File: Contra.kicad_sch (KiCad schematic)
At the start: 100 parts, among them J1 Conn_01x04, SW1 SW_PUSH, U1 ProMicro

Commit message: update keyswitch symbol
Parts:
- MX1, MX10, MX11, MX12, MX13, MX14, MX15, MX16, MX17, MX18, MX19, MX2, MX20, MX21, MX22, MX23, MX24, MX25, MX26, MX27, MX28, MX29, MX3, MX30, MX31, MX32, MX33, MX34, MX35, MX36, MX37, MX38, MX39, MX4, MX40, MX41, MX42, MX43, MX44, MX45, MX46, MX47, MX48, MX5, MX6, MX7, MX8, MX9: symbol MX_Alps_Hybrids:MX-1U -> keyboard_parts:KEYSW

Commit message: update keyswitch matrix
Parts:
- MX49: symbol MX_Alps_Hybrids:MX-2U -> keyboard_parts:KEYSW
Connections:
- net COL0: now also MX1.1, MX13.1, MX25.1, MX37.1
- net COL1: now also MX14.1, MX2.1, MX26.1, MX38.1
- net COL10: now also MX11.1, MX23.1, MX35.1, MX47.1
- net COL11: now also MX12.1, MX24.1, MX36.1, MX48.1
- net COL2: now also MX15.1, MX27.1, MX3.1, MX39.1
- net COL3: now also MX16.1, MX28.1, MX4.1, MX40.1
- net COL4: now also MX17.1, MX29.1, MX41.1, MX5.1
- net COL5: now also MX18.1, MX30.1, MX42.1, MX6.1
- net COL6: now also MX19.1, MX31.1, MX43.1, MX7.1
- net COL7: now also MX20.1, MX32.1, MX44.1, MX8.1
- net COL8: now also MX21.1, MX33.1, MX45.1, MX9.1
- net COL9: now also MX10.1, MX22.1, MX34.1, MX46.1
- net at MX1.2: now also D1.2 (A)
- net at MX2.2: now also D2.2 (A)
- net at MX3.2: now also D3.2 (A)
- net at MX4.2: now also D4.2 (A)
- net at MX5.2: now also D5.2 (A)
- net at MX6.2: now also D6.2 (A)
- net at MX7.2: now also D7.2 (A)
- net at MX8.2: now also D8.2 (A)
- net at MX9.2: now also D9.2 (A)
- net at MX10.2: now also D10.2 (A)
- net at MX11.2: now also D11.2 (A)
- net at MX12.2: now also D12.2 (A)
- net at MX13.2: now also D13.2 (A)
- net at MX14.2: now also D14.2 (A)
- net at MX15.2: now also D15.2 (A)
- net at MX16.2: now also D16.2 (A)
- net at MX17.2: now also D17.2 (A)
- net at MX18.2: now also D18.2 (A)
- net at MX19.2: now also D19.2 (A)
- net at MX20.2: now also D20.2 (A)
- net at MX21.2: now also D21.2 (A)
- net at MX22.2: now also D22.2 (A)
- net at MX23.2: now also D23.2 (A)
- net at MX24.2: now also D24.2 (A)
- net at MX25.2: now also D25.2 (A)
- net at MX26.2: now also D26.2 (A)
- net at MX27.2: now also D27.2 (A)
- net at MX28.2: now also D28.2 (A)
- net at MX29.2: now also D29.2 (A)
- net at MX30.2: now also D30.2 (A)
- net at MX31.2: now also D31.2 (A)
- net at MX32.2: now also D32.2 (A)
- net at MX33.2: now also D33.2 (A)
- net at MX34.2: now also D34.2 (A)
- net at MX35.2: now also D35.2 (A)
- net at MX36.2: now also D36.2 (A)
- net at MX37.2: now also D37.2 (A)
- net at MX38.2: now also D38.2 (A)
- net at MX39.2: now also D39.2 (A)
- net at MX40.2: now also D40.2 (A)
- net at MX41.2: now also D41.2 (A)
- net at MX42.2: now also D42.2 (A)
- net at MX43.2: now also D43.2 (A)
- net at MX44.2: now also D44.2 (A)
- net at MX45.2: now also D45.2 (A)
- net at MX46.2: now also D46.2 (A)
- net at MX47.2: now also D47.2 (A)
- net at MX48.2: now also D48.2 (A)
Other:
- note added: "Accessory Jumper"
- note added: "Keyswitch Matrix"
- note added: "MCU Connections"
- moved on the sheet: D1, D10, D11, D12, D13, D14, D15, D16, D17, D18, D19, D2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

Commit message: update foot prints to be hotswap sockets
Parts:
- D1, D10, D11, D12, D13, D14, D15, D16, D17, D18, D19, D2, D20, D21, D22, D23, D24, D25, D26, D27, D28, D29, D3, D30, D31, D32, D33, D34, D35, D36, D37, D38, D39, D4, D40, D41, D42, D43, D44, D45, D46, D47, D48, D5, D6, D7, D8, D9: footprint locallib:D_DO-35_SOD27_P7.62mm_Horizontal-DoubleSided -> Diode_THT:D_DO-35_SOD27_P7.62mm_Horizontal
- J1: footprint Pin_Headers:Pin_Header_Straight_1x04_Pitch2.54mm -> Connector_PinHeader_2.54mm:PinHeader_1x04_P2.54mm_Horizontal
- MX1, MX10, MX11, MX12, MX13, MX14, MX15, MX16, MX17, MX18, MX19, MX2, MX20, MX21, MX22, MX23, MX24, MX25, MX26, MX27, MX28, MX29, MX3, MX30, MX31, MX32, MX33, MX34, MX35, MX36, MX37, MX38, MX39, MX4, MX40, MX41, MX42, MX43, MX44, MX45, MX46, MX47, MX48, MX5, MX6, MX7, MX8, MX9: footprint MX_Alps_Hybrid:MX-1U-NoLED -> MX_Hotswap:MX-Hotswap-1U
- MX49: footprint MX_Alps_Hybrid:MX-2U-ReversedStabilizers-NoLED -> MX_Hotswap:MX-Hotswap-2U-ReversedStabilizers
- SW1: footprint Molex-0548190589:PushButton_6x6mm_TH_Pretty -> Button_Switch_THT:SW_PUSH_1P1T_6x3.5mm_H5.0_APEM_MJTP1250

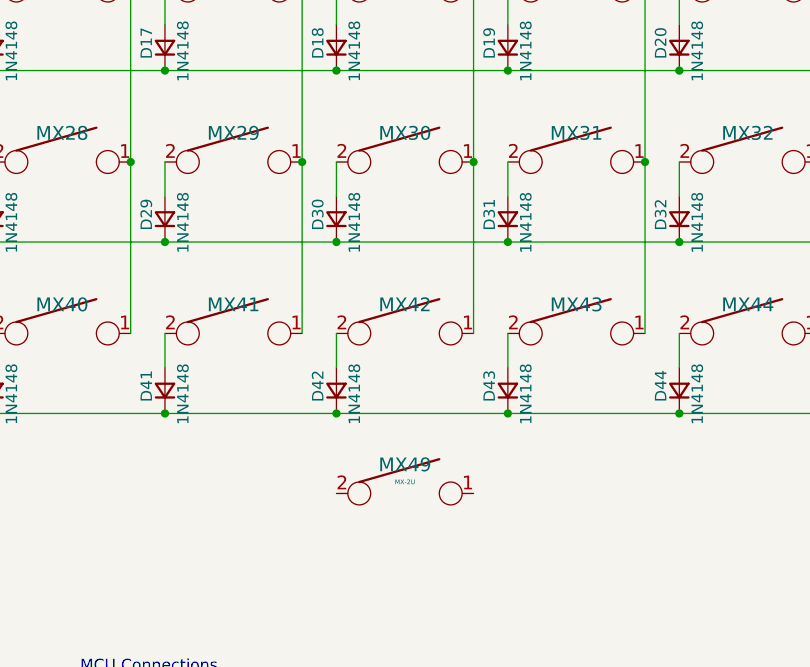
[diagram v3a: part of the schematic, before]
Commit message: place switch 49 in the correct place
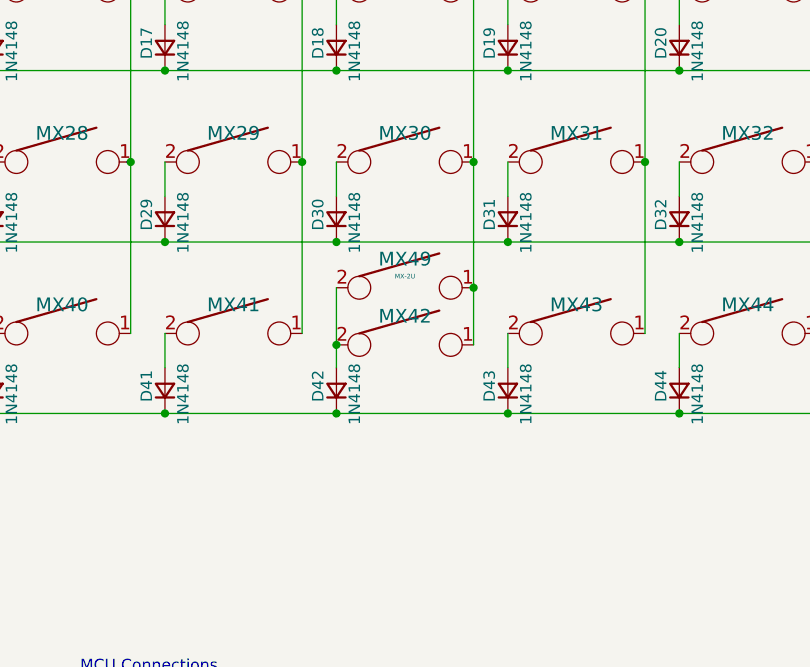
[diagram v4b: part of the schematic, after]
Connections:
- net COL5: now also MX49.1
- net at D42.2 (A), MX42.2: now also MX49.2
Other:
- moved on the sheet: MX42, MX49
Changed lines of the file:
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@@
 	)
 	(junction
+		(at 138.43 107.95)
+		(diameter 0)
+		(color 0 0 0 0)
+	)
+	(junction
 		(at 119.38 58.42)
 		(diameter 0)
@@
 	)
 	(junction
-		(at 153.67 87.63)
-		(diameter 0)
-		(color 0 0 0 0)
-	)
-	(junction
 		(at 115.57 49.53)
 		(diameter 0)
@@
 	)
 	(junction
+		(at 153.67 101.6)
+		(diameter 0)
+		(color 0 0 0 0)
+	)
+	(junction
 		(at 81.28 77.47)
 		(diameter 0)
@@
 	)
 	(junction
+		(at 153.67 87.63)
+		(diameter 0)
+		(color 0 0 0 0)
+	)
+	(junction
 		(at 43.18 77.47)
 		(diameter 0)
@@
 	(wire
 		(pts
-			(xy 138.43 106.68) (xy 138.43 110.49)
+			(xy 138.43 107.95) (xy 138.43 110.49)
 		)
 		(stroke
@@
 	(wire
 		(pts
-			(xy 153.67 87.63) (xy 153.67 106.68)
+			(xy 153.67 87.63) (xy 153.67 101.6)
 		)
 		(stroke
@@
 	(wire
 		(pts
+			(xy 138.43 101.6) (xy 138.43 107.95)
+		)
+		(stroke
+			(width 0)
+			(type default)
+		)
+	)
+	(wire
+		(pts
 			(xy 77.47 68.58) (xy 77.47 87.63)
 		)
@@
 	(wire
 		(pts
+			(xy 153.67 101.6) (xy 153.67 107.95)
+		)
+		(stroke
+			(width 0)
+			(type default)
+		)
+	)
+	(wire
+		(pts
 			(xy 119.38 115.57) (xy 138.43 115.57)
 		)
@@
 	(symbol
 		(lib_id "keyboard_parts:KEYSW")
-		(at 146.05 106.68 0)
+		(at 146.05 107.95 0)
 		(unit 1)
 		(body_style 1)
@@
 		(dnp no)
 		(property "Reference" "MX42"
-			(at 146.05 103.505 0)
+			(at 146.05 104.775 0)
 			(show_name no)
 			(do_not_autoplace no)
@@
 		)
 		(property "Value" "MX-1U"
-			(at 146.05 105.41 0)
+			(at 146.05 106.68 0)
 			(hide yes)
 			(show_name no)
@@
 		)
 		(property "Footprint" "MX_Hotswap:MX-Hotswap-1U"
-			(at 146.05 106.68 0)
+			(at 146.05 107.95 0)
 			(hide yes)
 			(show_name no)
@@
 		)
 		(property "Datasheet" ""
-			(at 146.05 106.68 0)
+			(at 146.05 107.95 0)
 			(hide yes)
 			(show_name no)
@@
 		)
 		(property "Description" ""
-			(at 146.05 106.68 0)
+			(at 146.05 107.95 0)
 			(hide yes)
 			(show_name no)
@@
 	(symbol
 		(lib_id "keyboard_parts:KEYSW")
-		(at 146.05 124.46 0)
+		(at 146.05 101.6 0)
 		(unit 1)
 		(body_style 1)
@@
 		(dnp no)
 		(property "Reference" "MX49"
-			(at 146.05 121.285 0)
+			(at 146.05 98.425 0)
 			(show_name no)
 			(do_not_autoplace no)
@@
 		)
 		(property "Value" "MX-2U"
-			(at 146.05 123.19 0)
+			(at 146.05 100.33 0)
 			(show_name no)
 			(do_not_autoplace no)
@@
 		)
 		(property "Footprint" "MX_Hotswap:MX-Hotswap-2U-ReversedStabilizers"
-			(at 146.05 124.46 0)
+			(at 146.05 101.6 0)
 			(hide yes)
 			(show_name no)
@@
 		)
 		(property "Datasheet" ""
-			(at 146.05 124.46 0)
+			(at 146.05 101.6 0)
 			(hide yes)
 			(show_name no)
@@
 		)
 		(property "Description" ""
-			(at 146.05 124.46 0)
+			(at 146.05 101.6 0)
 			(hide yes)
 			(show_name no)

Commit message: tweaking placements
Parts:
- J1: footprint Connector_PinHeader_2.54mm:PinHeader_1x04_P2.54mm_Horizontal -> Connector_PinHeader_2.54mm:PinHeader_1x04_P2.54mm_Vertical
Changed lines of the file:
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@@
 			)
 		)
-		(property "Footprint" "Connector_PinHeader_2.54mm:PinHeader_1x04_P2.54mm_Horizontal"
+		(property "Footprint" "Connector_PinHeader_2.54mm:PinHeader_1x04_P2.54mm_Vertical"
 			(at 45.72 152.4 0)
 			(hide yes)

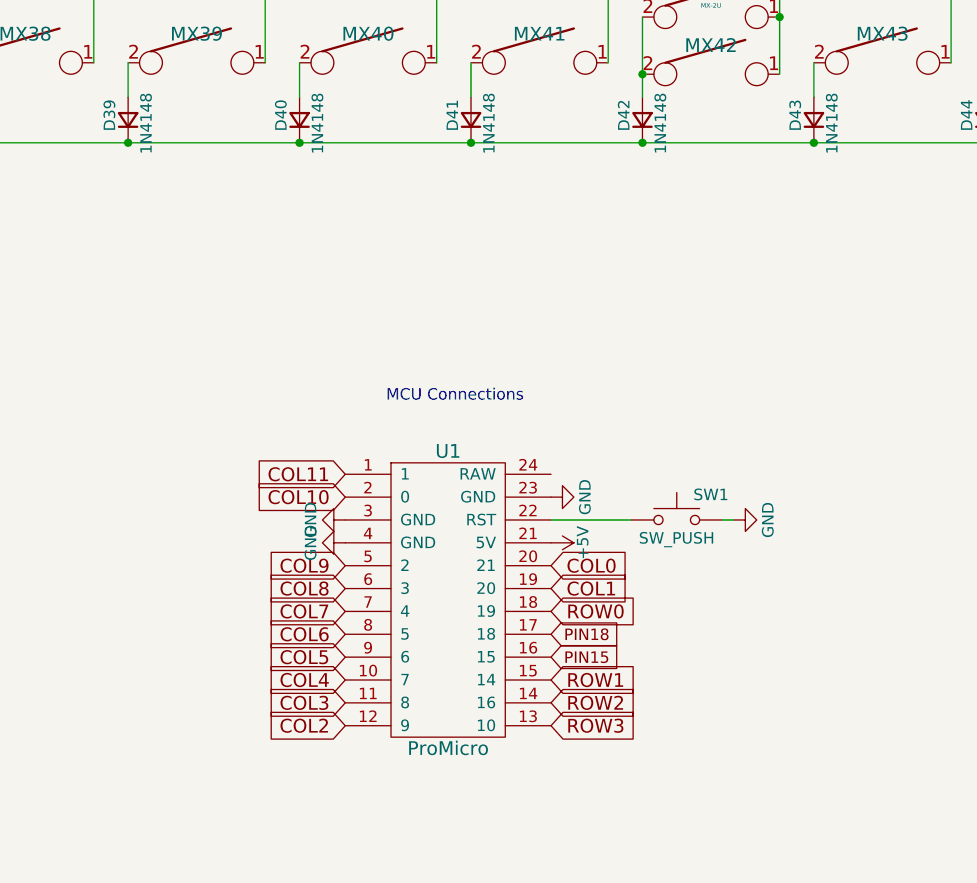
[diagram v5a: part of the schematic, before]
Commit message: udpate promicro symbol and footprint
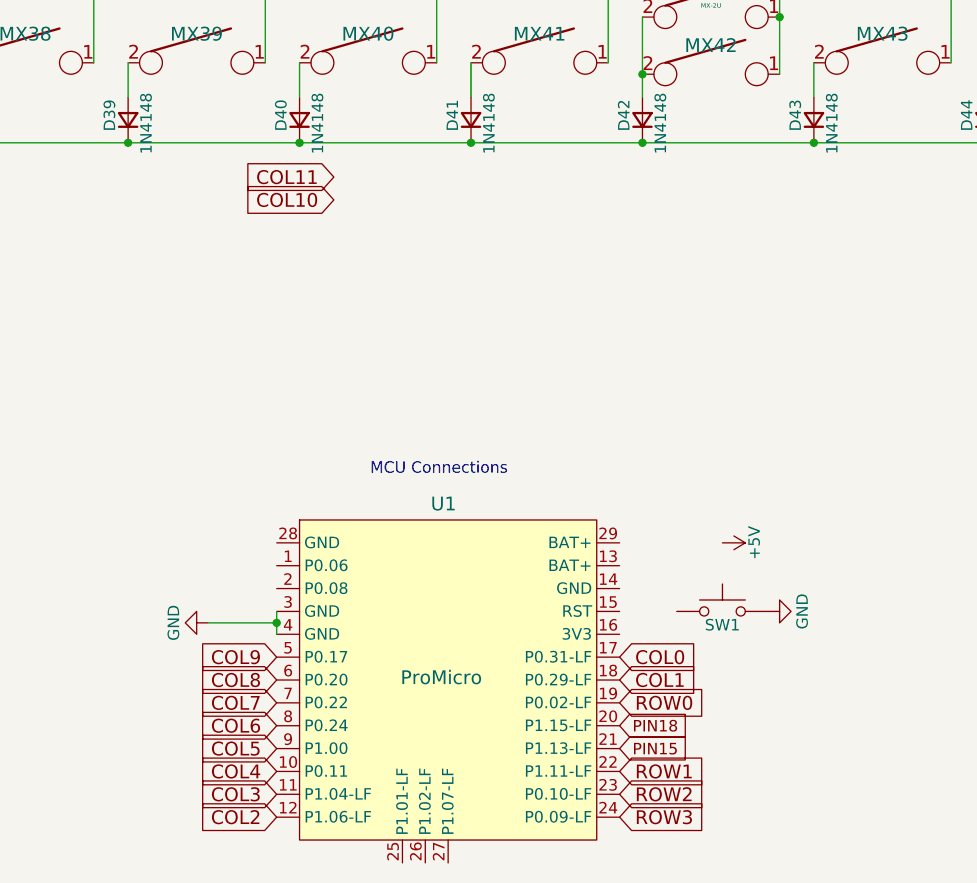
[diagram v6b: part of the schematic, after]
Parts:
- U1: footprint locallib:pro_micro -> PCM_marbastlib-xp-promicroish:nice_nano_AH_USBup; symbol josh:ProMicro -> Reilly_Components:nice_nano; now left out of the parts list
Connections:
- net +5V: no longer U1.21 (5V)
- net COL0: now also U1.17 (P0.31-LF); no longer U1.20 (21)
- net COL1: now also U1.18 (P0.29-LF); no longer U1.19 (20)
- net COL10: no longer U1.2 (0)
- net COL11: no longer U1.1
- net GND: no longer U1.23 (GND)
- net PIN15: now also U1.21 (P1.13-LF); no longer U1.16 (15)
- net PIN18: now also U1.20 (P1.15-LF); no longer U1.17 (18)
- net ROW0: now also U1.19 (P0.02-LF); no longer U1.18 (19)
- net ROW1: now also U1.22 (P1.11-LF); no longer U1.15 (14)
- net ROW2: now also U1.23 (P0.10-LF); no longer U1.14 (16)
- net ROW3: now also U1.24 (P0.09-LF); no longer U1.13 (10)
- net at SW1.1: no longer U1.22 (RST)
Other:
- moved on the sheet: SW1

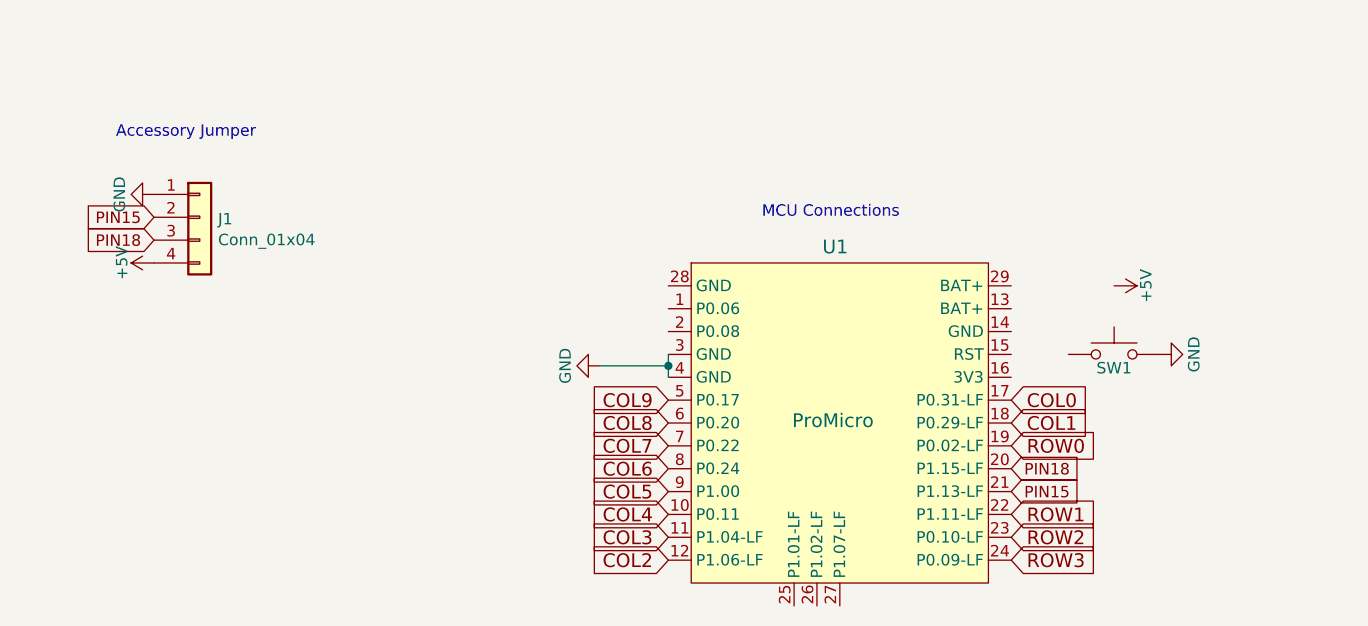
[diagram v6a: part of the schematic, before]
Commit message: update pin connections for nice!nano v2
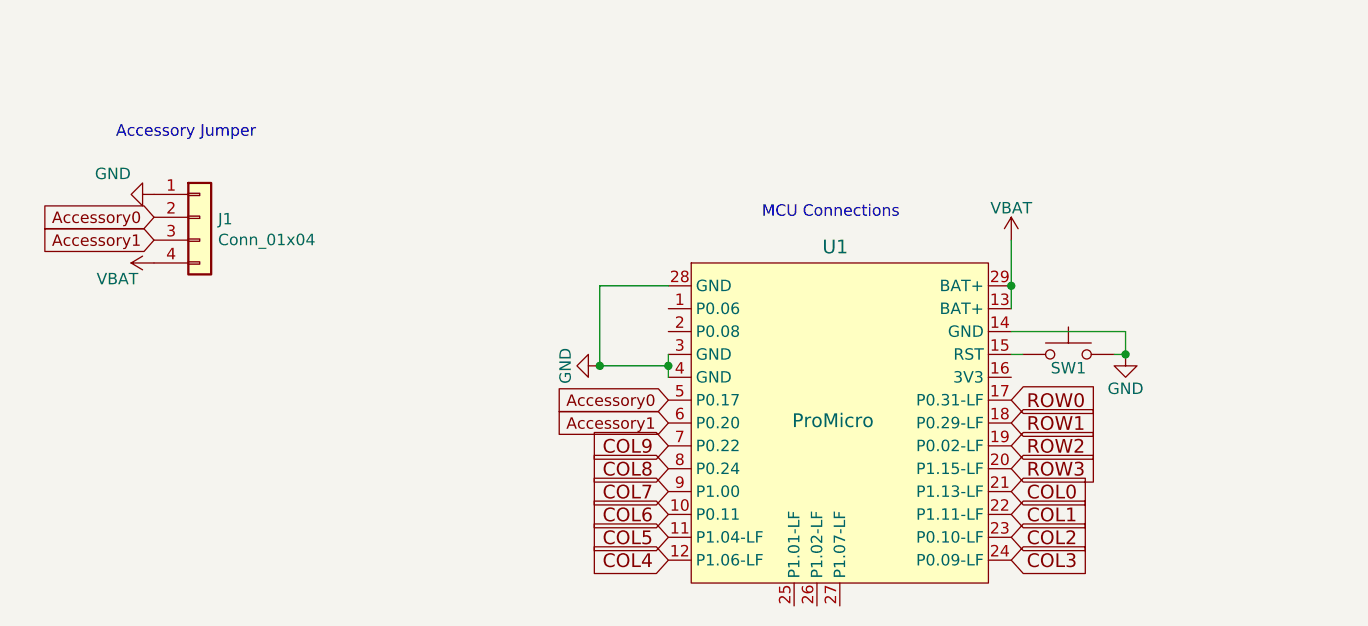
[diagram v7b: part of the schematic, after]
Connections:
- net +5V is gone; now on net VBAT: J1.4 (Pin_4)
- net COL0: now also U1.21 (P1.13-LF); no longer U1.17 (P0.31-LF)
- net COL1: now also U1.22 (P1.11-LF); no longer U1.18 (P0.29-LF)
- net COL2: now also U1.23 (P0.10-LF); no longer U1.12 (P1.06-LF)
- net COL3: now also U1.24 (P0.09-LF); no longer U1.11 (P1.04-LF)
- net COL4: now also U1.12 (P1.06-LF); no longer U1.10 (P0.11)
- net COL5: now also U1.11 (P1.04-LF); no longer U1.9 (P1.00)
- net COL6: now also U1.10 (P0.11); no longer U1.8 (P0.24)
- net COL7: now also U1.9 (P1.00); no longer U1.7 (P0.22)
- net COL8: now also U1.8 (P0.24); no longer U1.6 (P0.20)
- net COL9: now also U1.7 (P0.22); no longer U1.5 (P0.17)
- net GND: now also U1.14 (GND), U1.28 (GND)
- net ROW0: now also U1.17 (P0.31-LF); no longer U1.19 (P0.02-LF)
- net ROW1: now also U1.18 (P0.29-LF); no longer U1.22 (P1.11-LF)
- net ROW2: now also U1.19 (P0.02-LF); no longer U1.23 (P0.10-LF)
- net ROW3: now also U1.20 (P1.15-LF); no longer U1.24 (P0.09-LF)
- net VBAT: now reaches U1.13 (BAT+)
- net VBAT: now also U1.29 (BAT+)
- net at U1.15 (RST): now also SW1.1
- net PIN15 renamed Accessory0
- net Accessory0: now also U1.5 (P0.17); no longer U1.21 (P1.13-LF)
- net PIN18 renamed Accessory1
- net Accessory1: now also U1.6 (P0.20); no longer U1.20 (P1.15-LF)
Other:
- moved on the sheet: SW1

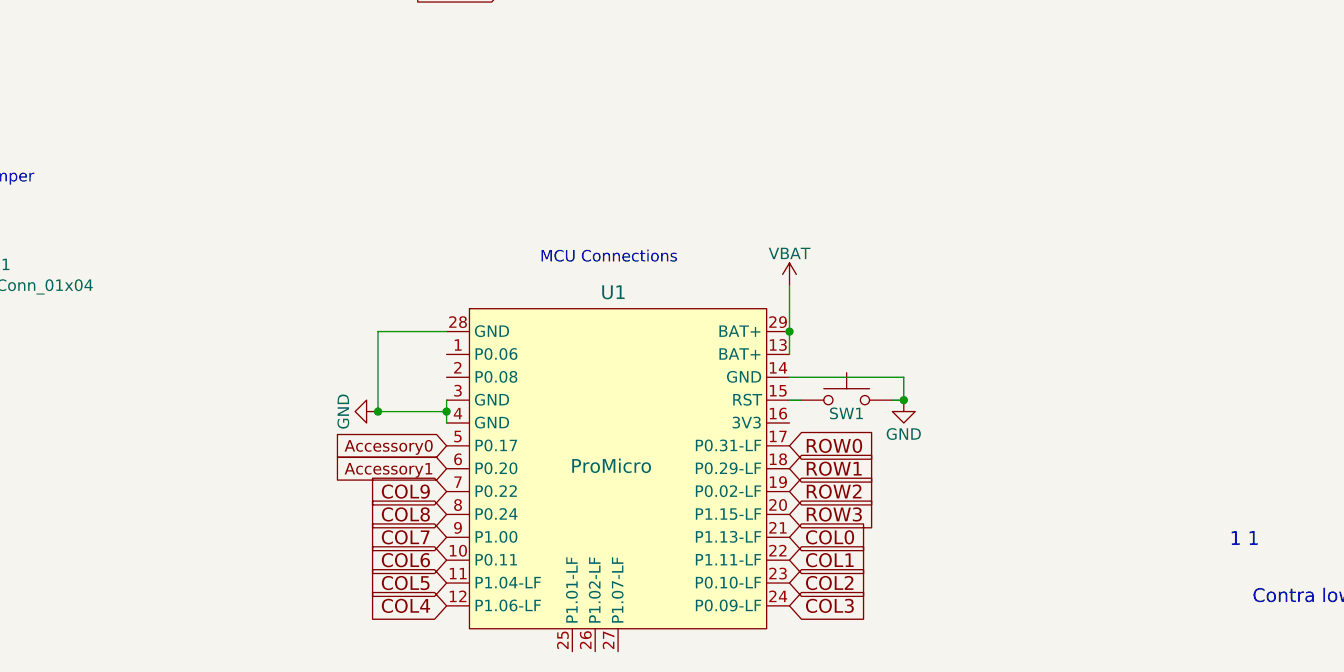
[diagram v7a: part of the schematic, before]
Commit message: add in batter connector and switch
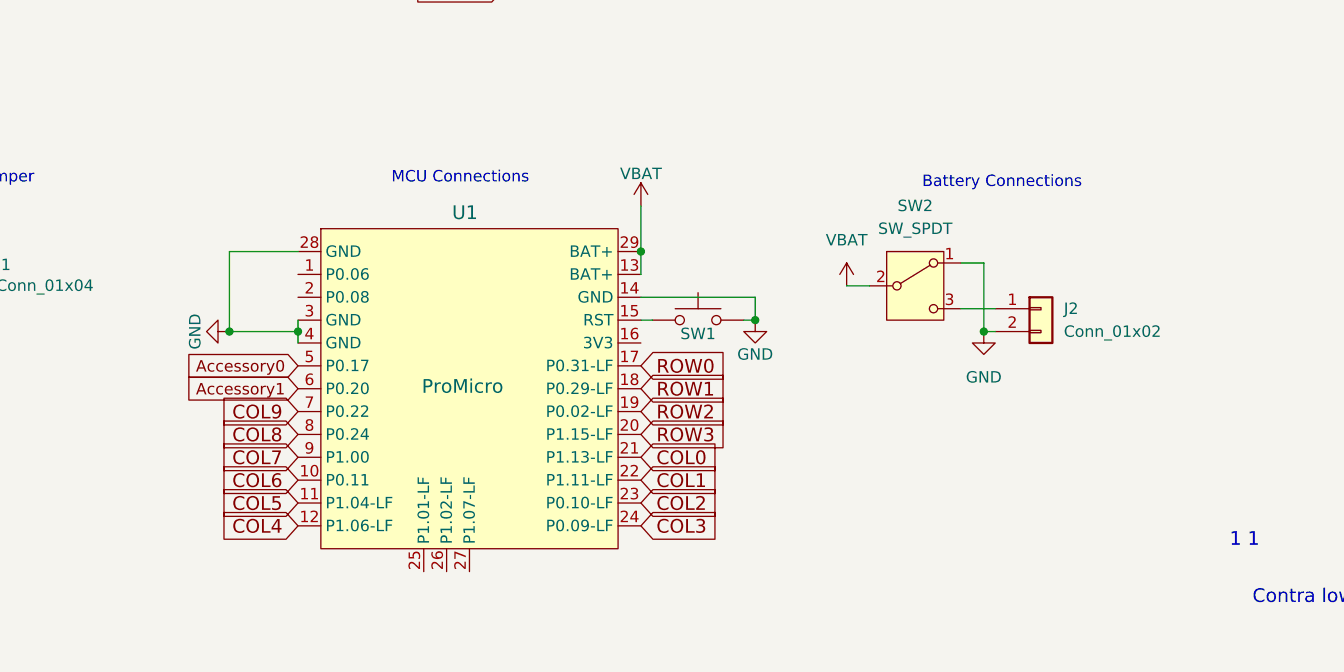
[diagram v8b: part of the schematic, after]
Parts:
- added J2: Conn_01x02, Connector_JST:JST_XH_S2B-XH-A_1x02_P2.50mm_Horizontal, symbol Connector_Generic:Conn_01x02
- added SW2: SW_SPDT, Button_Switch_THT:SW_Slide_SPDT_Angled_CK_OS102011MA1Q, symbol Switch:SW_SPDT
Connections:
- net GND: now also J2.2 (Pin_2), SW2.1 (A)
- net VBAT: now also SW2.2 (B)
- new net: J2.1 (Pin_1), SW2.3 (C)
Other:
- note added: "Battery Connections"
- moved on the sheet: SW1, U1
